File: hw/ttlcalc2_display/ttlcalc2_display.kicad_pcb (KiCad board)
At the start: 2 copper layers, 167.6 x 177.8 mm, 186 parts, among them J1 DISP_CONN, J2 IO_BUS, J3 5V_PWR, J4 HV_PWR, Q1 MPSA42, Q10 MPSA42, Q11 MPSA42, Q12 MPSA42, Q13 MPSA42, Q14 MPSA42, Q15 MPSA42, Q16 MPSA42, Q17 MPSA42, Q18 MPSA42, Q19 MPSA42, Q2 MPSA42, Q20 MPSA42, Q21 MPSA42, Q22 MPSA42, Q23 MPSA42, Q24 MPSA42, Q25 MPSA42, Q26 MPSA42, Q27 MPSA42, Q28 MPSA42, Q29 MPSA42, Q3 MPSA42, Q30 MPSA92, Q31 MPSA92, Q32 MPSA92, Q33 MPSA42, Q34 MPSA42, Q35 MPSA42, Q36 MPSA92, Q37 MPSA92, Q38 MPSA92, Q39 MPSA42, Q4 MPSA42, Q40 MPSA42, Q41 MPSA42, Q42 MPSA92, Q43 MPSA92, Q44 MPSA92, Q45 MPSA42, Q46 MPSA42, Q47 MPSA42, Q48 MPSA92, Q49 MPSA92, Q5 MPSA42, Q50 MPSA92, Q51 MPSA42, Q52 MPSA42, Q53 MPSA92, Q54 MPSA92, Q6 MPSA42, Q7 MPSA42, Q8 MPSA42, Q9 MPSA42, U1 74LS138, U10 74LS04, U11 74LS04, U12 74LS42, U13 74LS04, U14 74LS04, U15 74LS138, U16 74LS138, U17 74LS04, U18 74LS04, U19 74LS04, U2 74LS138, U3 74LS173, U4 74LS173, U5 74LS173, U6 74LS08, U7 74LS173, U8 74LS138, U9 74LS138

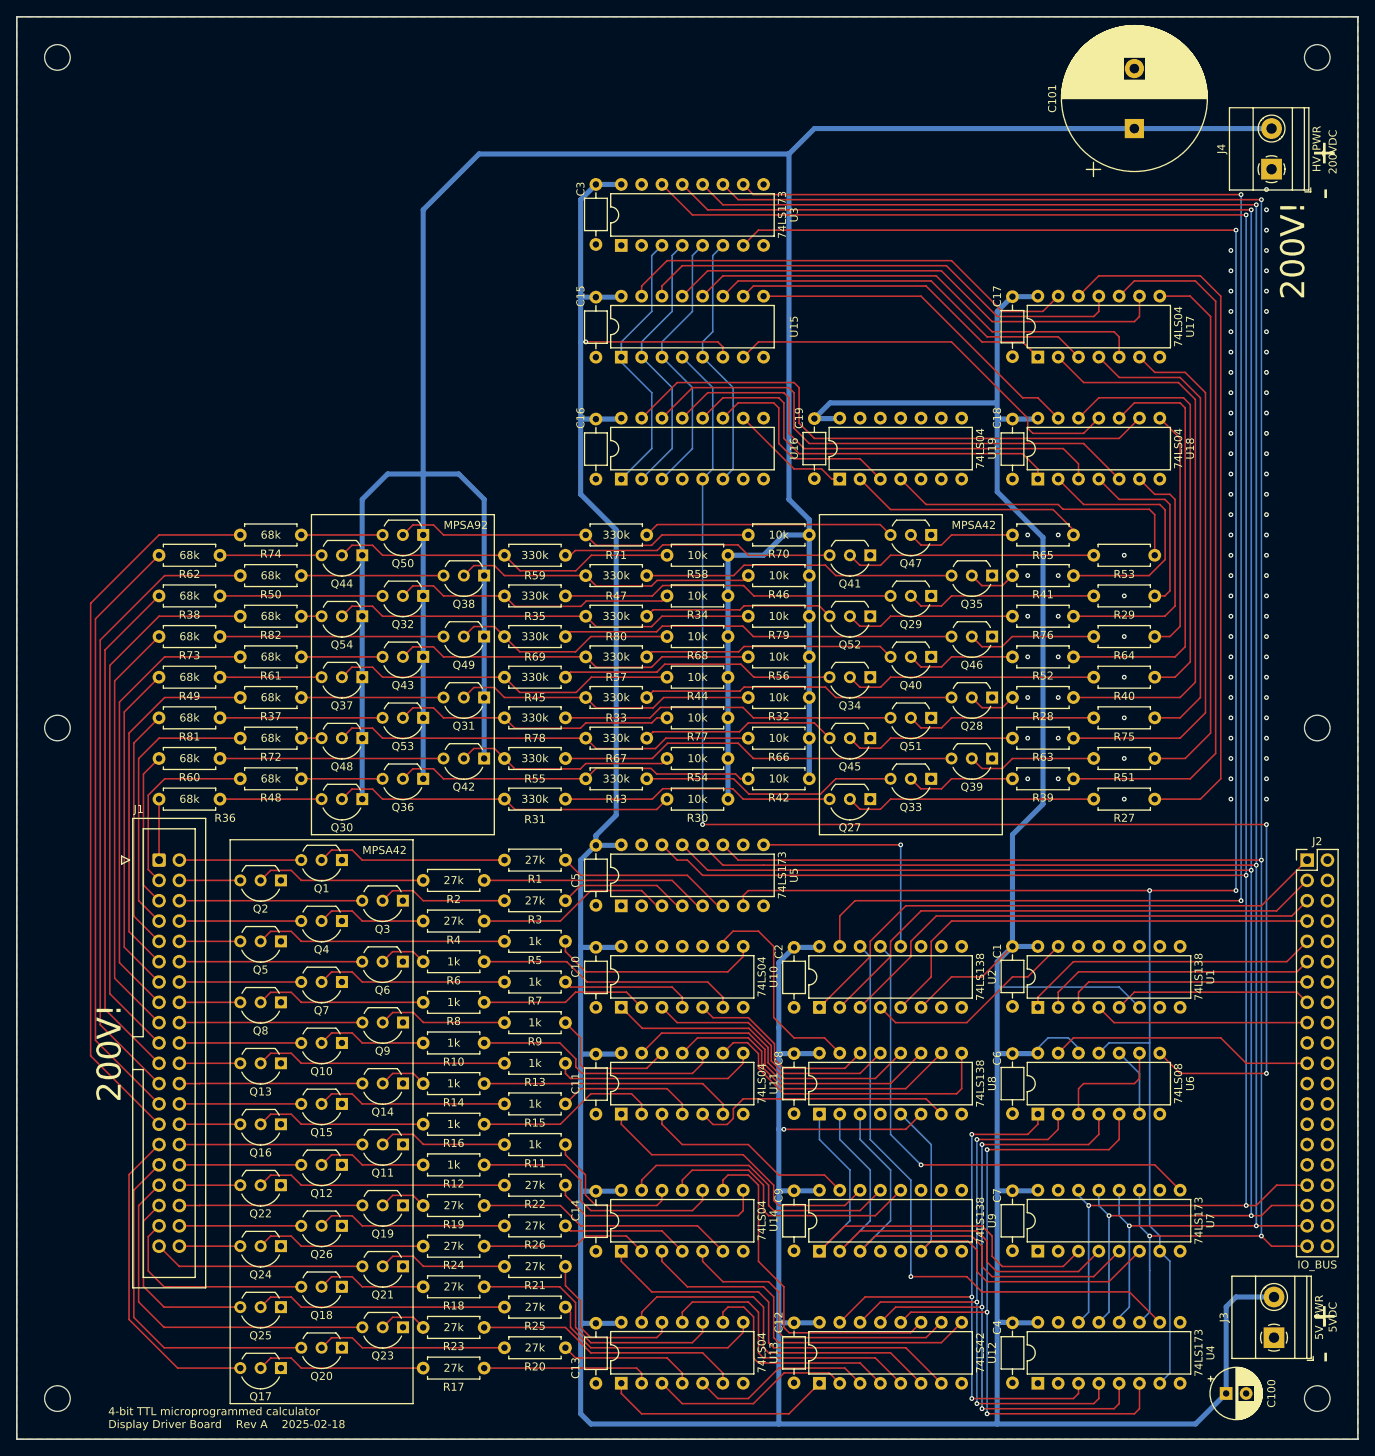
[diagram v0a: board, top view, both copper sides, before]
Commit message: Display driver geographical reannotate
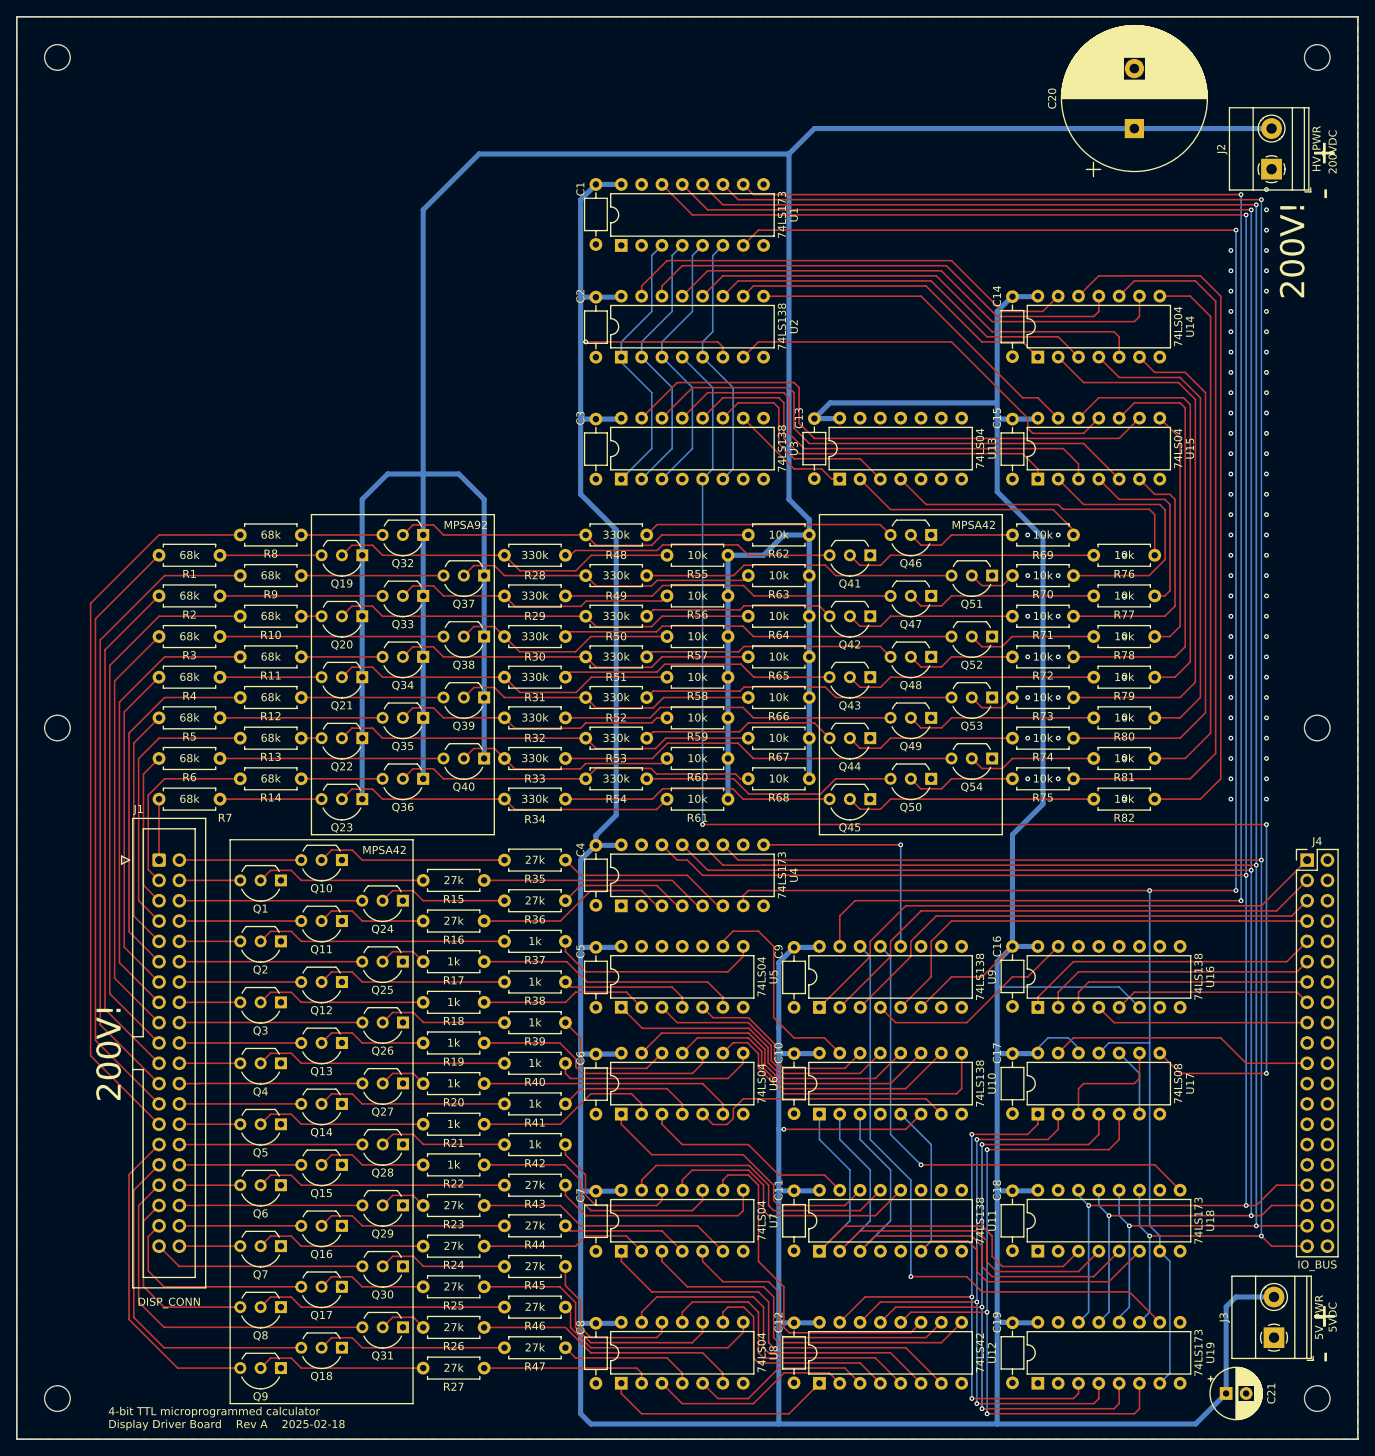
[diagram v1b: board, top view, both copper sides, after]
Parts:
- renumbered C3 to C1, C8 to C10, C9 to C11, C19 to C13, C17 to C14, C18 to C15, C1 to C16, C6 to C17, C7 to C18, C4 to C19, C15 to C2, C101 to C20, C100 to C21, C16 to C3, C5 to C4, C10 to C5, C11 to C6, C14 to C7, C13 to C8, C2 to C9, H6 to H4, H4 to H6, J4 to J2, J2 to J4, Q2 to Q1, Q1 to Q10, Q4 to Q11, Q7 to Q12, Q10 to Q13, Q15 to Q14, Q12 to Q15, Q26 to Q16, Q18 to Q17, Q20 to Q18, Q44 to Q19, Q5 to Q2, Q54 to Q20, Q37 to Q21, Q48 to Q22, Q30 to Q23, Q3 to Q24, Q6 to Q25, Q9 to Q26, Q14 to Q27, Q11 to Q28, Q19 to Q29, Q8 to Q3, Q21 to Q30, Q23 to Q31, Q50 to Q32, Q32 to Q33, Q43 to Q34, Q53 to Q35, Q38 to Q37, Q49 to Q38, Q31 to Q39, Q13 to Q4, Q42 to Q40, Q52 to Q42, Q34 to Q43, Q45 to Q44, Q27 to Q45, Q47 to Q46, Q29 to Q47, Q40 to Q48, Q51 to Q49, Q16 to Q5, Q33 to Q50, Q35 to Q51, Q46 to Q52, Q28 to Q53, Q39 to Q54, Q22 to Q6, Q24 to Q7, Q25 to Q8, Q17 to Q9, R62 to R1, R82 to R10, R61 to R11, R37 to R12, R72 to R13, R48 to R14, R2 to R15, R4 to R16, R6 to R17, R8 to R18, R10 to R19, R38 to R2, R14 to R20, R16 to R21, R12 to R22, R19 to R23, R18 to R25, R23 to R26, R17 to R27, R59 to R28, R35 to R29, R73 to R3, R69 to R30, R45 to R31, R78 to R32, R55 to R33, R31 to R34, R1 to R35, R3 to R36, R5 to R37, R7 to R38, R9 to R39, R49 to R4, R13 to R40, R15 to R41, R11 to R42, R22 to R43, R26 to R44, R21 to R45, R25 to R46, R20 to R47, R71 to R48, R47 to R49, R81 to R5, R80 to R50, R57 to R51, R33 to R52, R67 to R53, R43 to R54, R58 to R55, R34 to R56, R68 to R57, R44 to R58, R77 to R59, R60 to R6, R54 to R60, R30 to R61, R70 to R62, R46 to R63, R79 to R64, R56 to R65, R32 to R66, R66 to R67, R42 to R68, R65 to R69, R36 to R7, R41 to R70, R76 to R71, R52 to R72, R28 to R73, R63 to R74, R39 to R75, R53 to R76, R29 to R77, R64 to R78, R40 to R79, R74 to R8, R75 to R80, R51 to R81, R27 to R82, R50 to R9, U3 to U1, U8 to U10, U9 to U11, U19 to U13, U17 to U14, U18 to U15, U1 to U16, U6 to U17, U7 to U18, U4 to U19, U15 to U2, U16 to U3, U5 to U4, U10 to U5, U11 to U6, U14 to U7, U13 to U8, U2 to U9

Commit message: Convert to KiCad 9.0
Convert to KiCad 9.0 format
Tweak silkscreen to fix DRC errors introduced by updated footprints
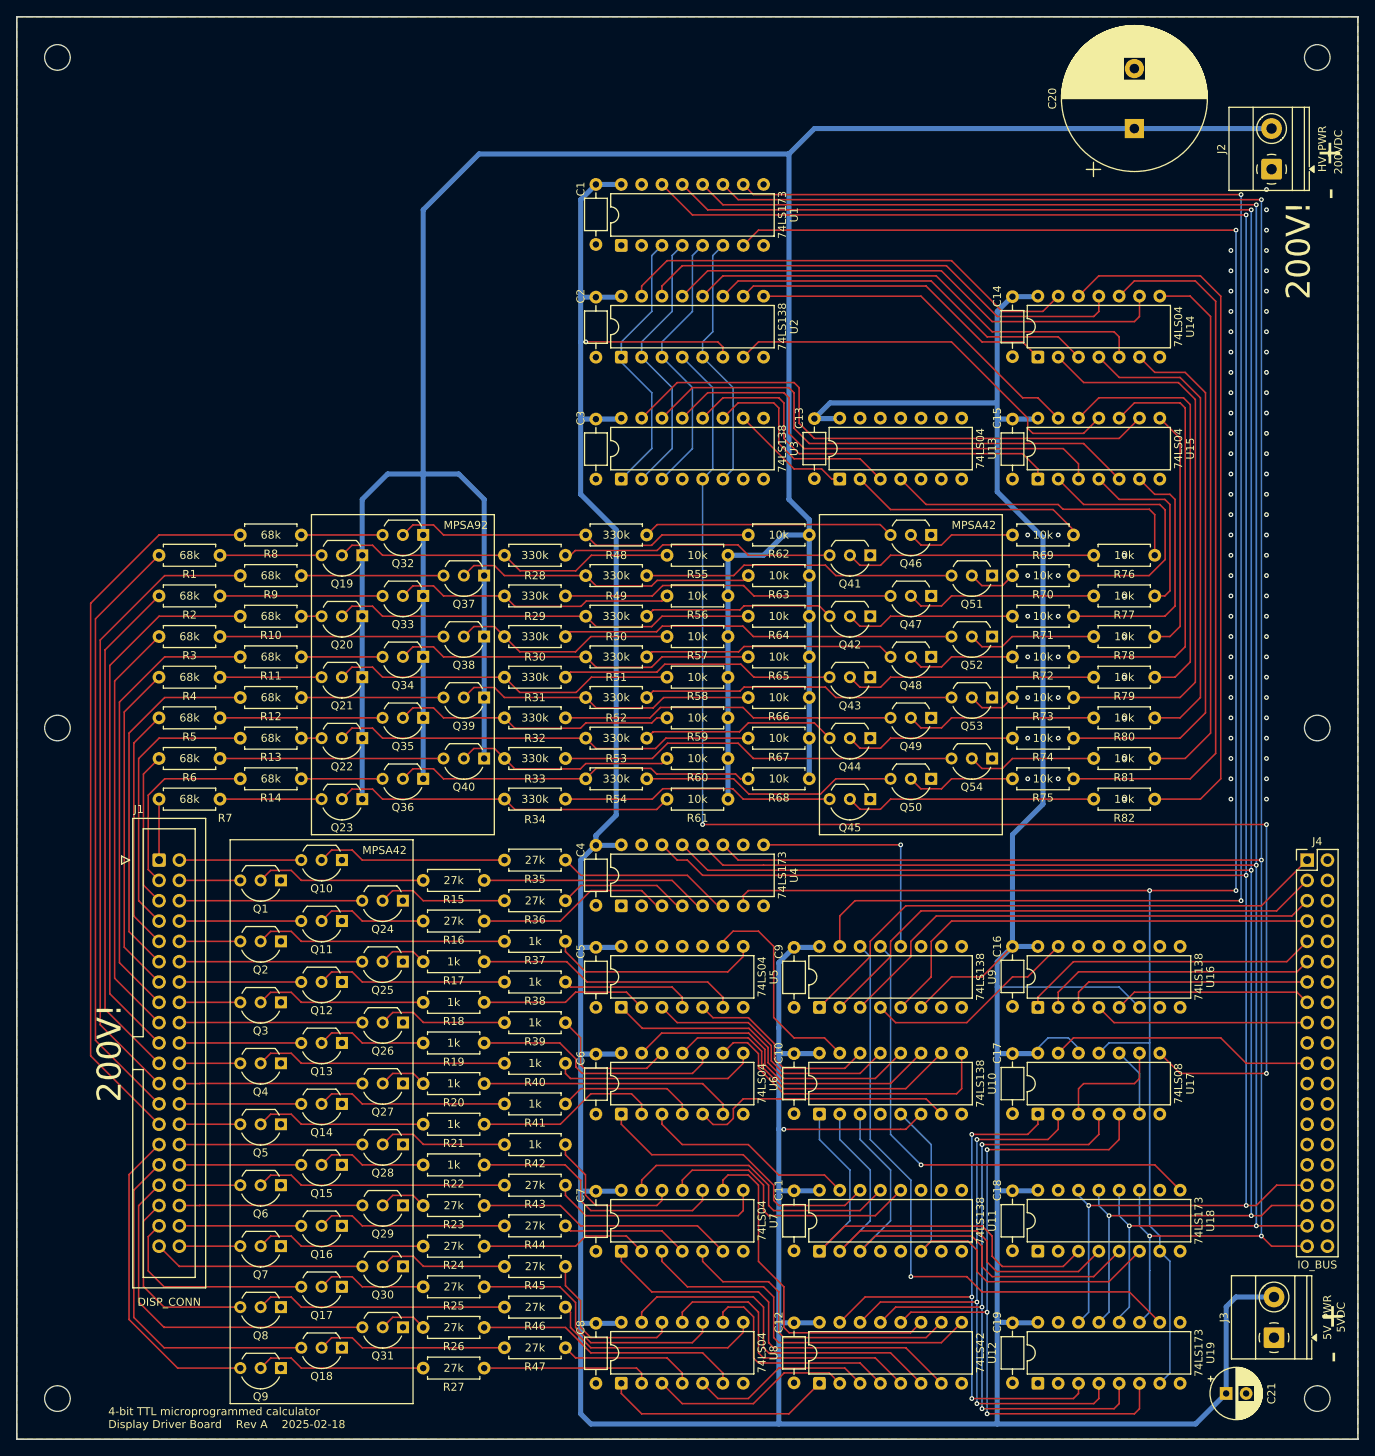
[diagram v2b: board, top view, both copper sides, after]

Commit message: Minor display hardware revisions
Add anti-ghosting inter-cathode resistors to nixies
Adjust component values based on experiments
Change from individual netclass labels to rule areas
Tweak traces on display board
Update .gitignore to ignore KiCad lock files
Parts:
- C1, C10, C11, C12, C13, C14, C15, C16, C17, C18, C19, C2, C3, C4, C5, C6, C7, C8, C9: value C -> 100n
- R1, R10, R11, R12, R13, R14, R2, R3, R4, R5, R6, R7, R8, R9: value 68k -> 10k
- R15, R16, R35, R36: value 27k -> 10k
- R17, R18, R19, R20, R21, R22, R37, R38, R39, R40, R41, R42: value 1k -> 10k
- R23, R24, R25, R26, R27, R43, R44, R45, R46, R47: value 27k -> 6.8k
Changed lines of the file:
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@@
 			)
 		)
-		(property "Value" "68k"
+		(property "Value" "10k"
 			(at 3.81 0 0)
 			(layer "F.SilkS")
@@
 			)
 		)
-		(property "Value" "C"
+		(property "Value" "100n"
 			(at 3.75 2.42 270)
 			(layer "F.Fab")
@@
 			)
 		)
-		(property "Value" "1k"
+		(property "Value" "10k"
 			(at 3.81 0 0)
 			(layer "F.SilkS")
@@
 			)
 		)
-		(property "Value" "27k"
+		(property "Value" "6.8k"
 			(at 3.81 0 0)
 			(layer "F.SilkS")
@@
 			)
 		)
-		(property "Value" "C"
+		(property "Value" "100n"
 			(at 3.75 2.42 90)
 			(layer "F.Fab")
@@
 			)
 		)
-		(property "Value" "C"
+		(property "Value" "100n"
 			(at 3.75 2.42 90)
 			(layer "F.Fab")
@@
 			)
 		)
-		(property "Value" "68k"
+		(property "Value" "10k"
 			(at 3.81 0 0)
 			(layer "F.SilkS")
@@
 			)
 		)
-		(property "Value" "C"
+		(property "Value" "100n"
 			(at 3.75 2.42 90)
 			(layer "F.Fab")
@@
 			)
 		)
-		(property "Value" "C"
+		(property "Value" "100n"
 			(at 3.75 2.42 270)
 			(layer "F.Fab")
@@
 			)
 		)
-		(property "Value" "27k"
+		(property "Value" "6.8k"
 			(at 3.81 0 0)
 			(layer "F.SilkS")
@@
 			)
 		)
-		(property "Value" "27k"
+		(property "Value" "10k"
 			(at 3.81 0 0)
 			(layer "F.SilkS")
@@
 			)
 		)
-		(property "Value" "C"
+		(property "Value" "100n"
 			(at 3.75 2.42 90)
 			(layer "F.Fab")
@@
 			)
 		)
-		(property "Value" "1k"
+		(property "Value" "10k"
 			(at 3.81 0 0)
 			(layer "F.SilkS")
@@
 			)
 		)
-		(property "Value" "1k"
+		(property "Value" "10k"
 			(at 3.81 0 0)
 			(layer "F.SilkS")
@@
 			)
 		)
-		(property "Value" "68k"
+		(property "Value" "10k"
 			(at 3.81 0 0)
 			(layer "F.SilkS")
@@
 			)
 		)
-		(property "Value" "C"
+		(property "Value" "100n"
 			(at 3.75 2.42 270)
 			(layer "F.Fab")
@@
 			)
 		)
-		(property "Value" "1k"
+		(property "Value" "10k"
 			(at 3.81 0 0)
 			(layer "F.SilkS")
@@
 			)
 		)
-		(property "Value" "C"
+		(property "Value" "100n"
 			(at 3.75 2.42 90)
 			(layer "F.Fab")
@@
 			)
 		)
-		(property "Value" "27k"
+		(property "Value" "10k"
 			(at 3.81 0 0)
 			(layer "F.SilkS")
@@
 			)
 		)
-		(property "Value" "C"
+		(property "Value" "100n"
 			(at 3.75 2.42 90)
 			(layer "F.Fab")
@@
 			)
 		)
-		(property "Value" "C"
+		(property "Value" "100n"
 			(at 3.75 2.42 270)
 			(layer "F.Fab")
@@
 			)
 		)
-		(property "Value" "1k"
+		(property "Value" "10k"
 			(at 3.81 0 0)
 			(layer "F.SilkS")
@@
 			)
 		)
-		(property "Value" "27k"
+		(property "Value" "6.8k"
 			(at 3.81 0 0)
 			(layer "F.SilkS")
@@
 			)
 		)
-		(property "Value" "27k"
+		(property "Value" "10k"
 			(at 3.81 0 0)
 			(layer "F.SilkS")
@@
 			)
 		)
-		(property "Value" "68k"
+		(property "Value" "10k"
 			(at 3.81 0 0)
 			(layer "F.SilkS")
@@
 			)
 		)
-		(property "Value" "C"
+		(property "Value" "100n"
 			(at 3.75 2.42 90)
 			(layer "F.Fab")
@@
 			)
 		)
-		(property "Value" "27k"
+		(property "Value" "6.8k"
 			(at 3.81 0 0)
 			(layer "F.SilkS")
@@
 			)
 		)
-		(property "Value" "C"
+		(property "Value" "100n"
 			(at 3.75 2.42 90)
 			(layer "F.Fab")
@@
 			)
 		)
-		(property "Value" "C"
+		(property "Value" "100n"
 			(at 3.75 2.42 90)
 			(layer "F.Fab")
@@
 			)
 		)
-		(property "Value" "C"
+		(property "Value" "100n"
 			(at 3.75 2.42 90)
 			(layer "F.Fab")
@@
 			)
 		)
-		(property "Value" "68k"
+		(property "Value" "10k"
 			(at 3.81 0 0)
 			(layer "F.SilkS")
@@
 			)
 		)
-		(property "Value" "1k"
+		(property "Value" "10k"
 			(at 3.81 0 0)
 			(layer "F.SilkS")
@@
 			)
 		)
-		(property "Value" "C"
+		(property "Value" "100n"
 			(at 3.75 2.42 270)
 			(layer "F.Fab")
@@
 			)
 		)
-		(property "Value" "68k"
+		(property "Value" "10k"
 			(at 3.81 0 0)
 			(layer "F.SilkS")
@@
 			)
 		)
-		(property "Value" "68k"
+		(property "Value" "10k"
 			(at 3.81 0 0)
 			(layer "F.SilkS")
@@
 			)
 		)
-		(property "Value" "68k"
+		(property "Value" "10k"
 			(at 3.81 0 0)
 			(layer "F.SilkS")
@@
 			)
 		)
-		(property "Value" "68k"
+		(property "Value" "10k"
 			(at 3.81 0 0)
 			(layer "F.SilkS")
@@
 			)
 		)
-		(property "Value" "C"
+		(property "Value" "100n"
 			(at 3.75 2.42 90)
 			(layer "F.Fab")
@@
 			)
 		)
-		(property "Value" "27k"
+		(property "Value" "6.8k"
 			(at 3.81 0 0)
 			(layer "F.SilkS")
@@
 			)
 		)
-		(property "Value" "1k"
+		(property "Value" "10k"
 			(at 3.81 0 0)
 			(layer "F.SilkS")
@@
 			)
 		)
-		(property "Value" "68k"
+		(property "Value" "10k"
 			(at 3.81 0 0)
 			(layer "F.SilkS")
@@
 			)
 		)
-		(property "Value" "27k"
+		(property "Value" "10k"
 			(at 3.81 0 0)
 			(layer "F.SilkS")
@@
 			)
 		)
-		(property "Value" "1k"
+		(property "Value" "10k"
 			(at 3.81 0 0)
 			(layer "F.SilkS")
@@
 			)
 		)
-		(property "Value" "68k"
+		(property "Value" "10k"
 			(at 3.81 0 0)
 			(layer "F.SilkS")
@@
 			)
 		)
-		(property "Value" "68k"
+		(property "Value" "10k"
 			(at 3.81 0 0)
 			(layer "F.SilkS")
@@
 			)
 		)
-		(property "Value" "68k"
+		(property "Value" "10k"
 			(at 3.81 0 0)
 			(layer "F.SilkS")
@@
 			)
 		)
-		(property "Value" "27k"
+		(property "Value" "6.8k"
 			(at 3.81 0 0)
 			(layer "F.SilkS")
@@
 			)
 		)
-		(property "Value" "C"
+		(property "Value" "100n"
 			(at 3.75 2.42 90)
 			(layer "F.Fab")
@@
 			)
 		)
-		(property "Value" "27k"
+		(property "Value" "6.8k"
 			(at 3.81 0 0)
 			(layer "F.SilkS")
@@
 			)
 		)
-		(property "Value" "1k"
+		(property "Value" "10k"
 			(at 3.81 0 0)
 			(layer "F.SilkS")
@@
 			)
 		)
-		(property "Value" "27k"
+		(property "Value" "6.8k"
 			(at 3.81 0 0)
 			(layer "F.SilkS")
@@
 			)
 		)
-		(property "Value" "C"
+		(property "Value" "100n"
 			(at 3.75 2.42 90)
 			(layer "F.Fab")
@@
 			)
 		)
-		(property "Value" "27k"
+		(property "Value" "6.8k"
 			(at 3.81 0 0)
 			(layer "F.SilkS")
@@
 			)
 		)
-		(property "Value" "1k"
+		(property "Value" "10k"
 			(at 3.81 0 0)
 			(layer "F.SilkS")
@@
 			)
 		)
-		(property "Value" "68k"
+		(property "Value" "10k"
 			(at 3.81 0 0)
 			(layer "F.SilkS")
@@
 			)
 		)
-		(property "Value" "27k"
+		(property "Value" "6.8k"
 			(at 3.81 0 0)
 			(layer "F.SilkS")
@@
 			)
 		)
-		(property "Value" "1k"
+		(property "Value" "10k"
 			(at 3.81 0 0)
 			(layer "F.SilkS")
@@
 			)
 		)
-		(property "Value" "1k"
+		(property "Value" "10k"
 			(at 3.81 0 0)
 			(layer "F.SilkS")
@@
 			)
 		)
-		(property "Value" "C"
+		(property "Value" "100n"
 			(at 3.75 2.42 90)
 			(layer "F.Fab")
@@
 			(font
 				(size 3 3)
-				(thickness 0.2)
+				(thickness 0.375)
 			)
 			(justify bottom)
@@
 			(font
 				(size 3 3)
-				(thickness 0.2)
+				(thickness 0.375)
 			)
 			(justify bottom)
